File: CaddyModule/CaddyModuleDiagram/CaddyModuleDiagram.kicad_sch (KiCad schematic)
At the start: 6 parts, among them J3 Conn_01x04, J4 Conn_01x02, J5 Conn_01x06, U1 ESP32-DEVKIT-V1, U2 A4988_STEPPER_MOTOR_DRIVER_CA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, U3 VL53L0X

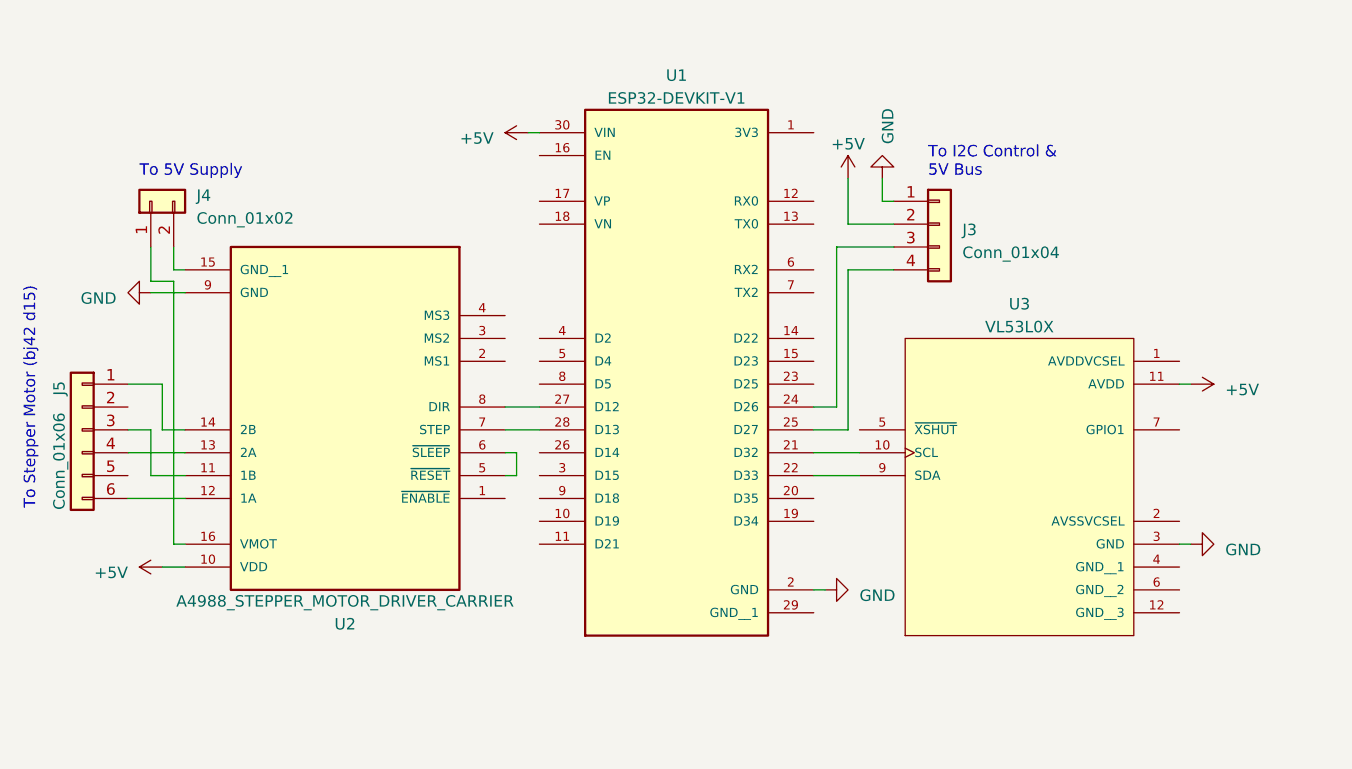
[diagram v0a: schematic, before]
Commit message: Adjusted caddy module to use RP2040 Pico
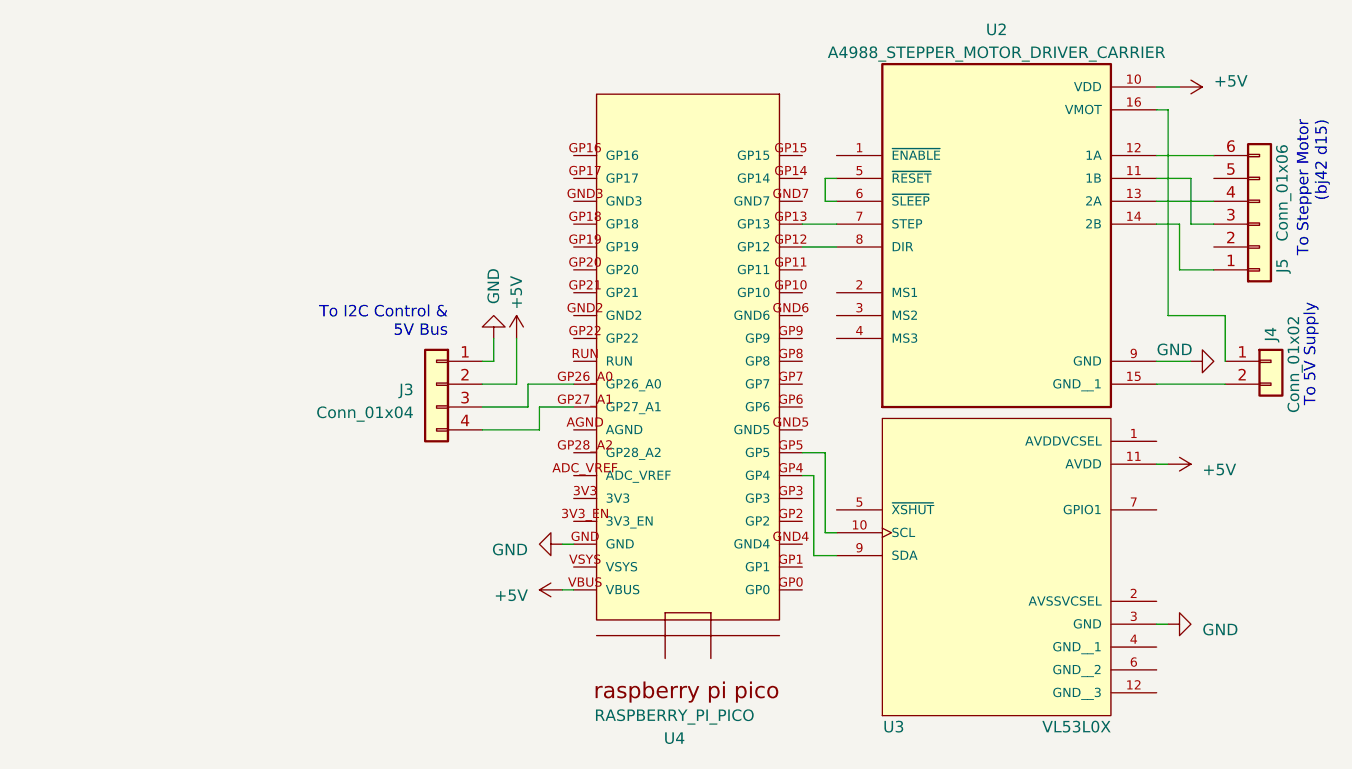
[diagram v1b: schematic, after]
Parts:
- removed U1: ESP32-DEVKIT-V1, SnapEDA Library:MODULE_ESP32_DEVKIT_V1, symbol ESP32-DEVKIT-V1:ESP32-DEVKIT-V1
- added U4: RASPBERRY_PI_PICO, RASPBERRY_PI_PICO:RASPBERRY_PI_PICO, symbol RASPBERRY_PI_PICO:RASPBERRY_PI_PICO
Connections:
- net +5V: now also U4.VBUS
- net GND: now also U4.GND
- net at U3.10 (SCL): now also U4.GP5
- net at U3.9 (SDA): now also U4.GP4
- net at J3.3 (Pin_3): now also U4.GP26_A0
- net at J3.4 (Pin_4): now also U4.GP27_A1
- net at U2.7 (STEP): now also U4.GP13
- net at U2.8 (DIR): now also U4.GP12
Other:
- moved on the sheet: J3, J4, J5, U2, U3
